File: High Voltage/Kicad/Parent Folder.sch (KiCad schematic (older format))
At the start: 45 parts

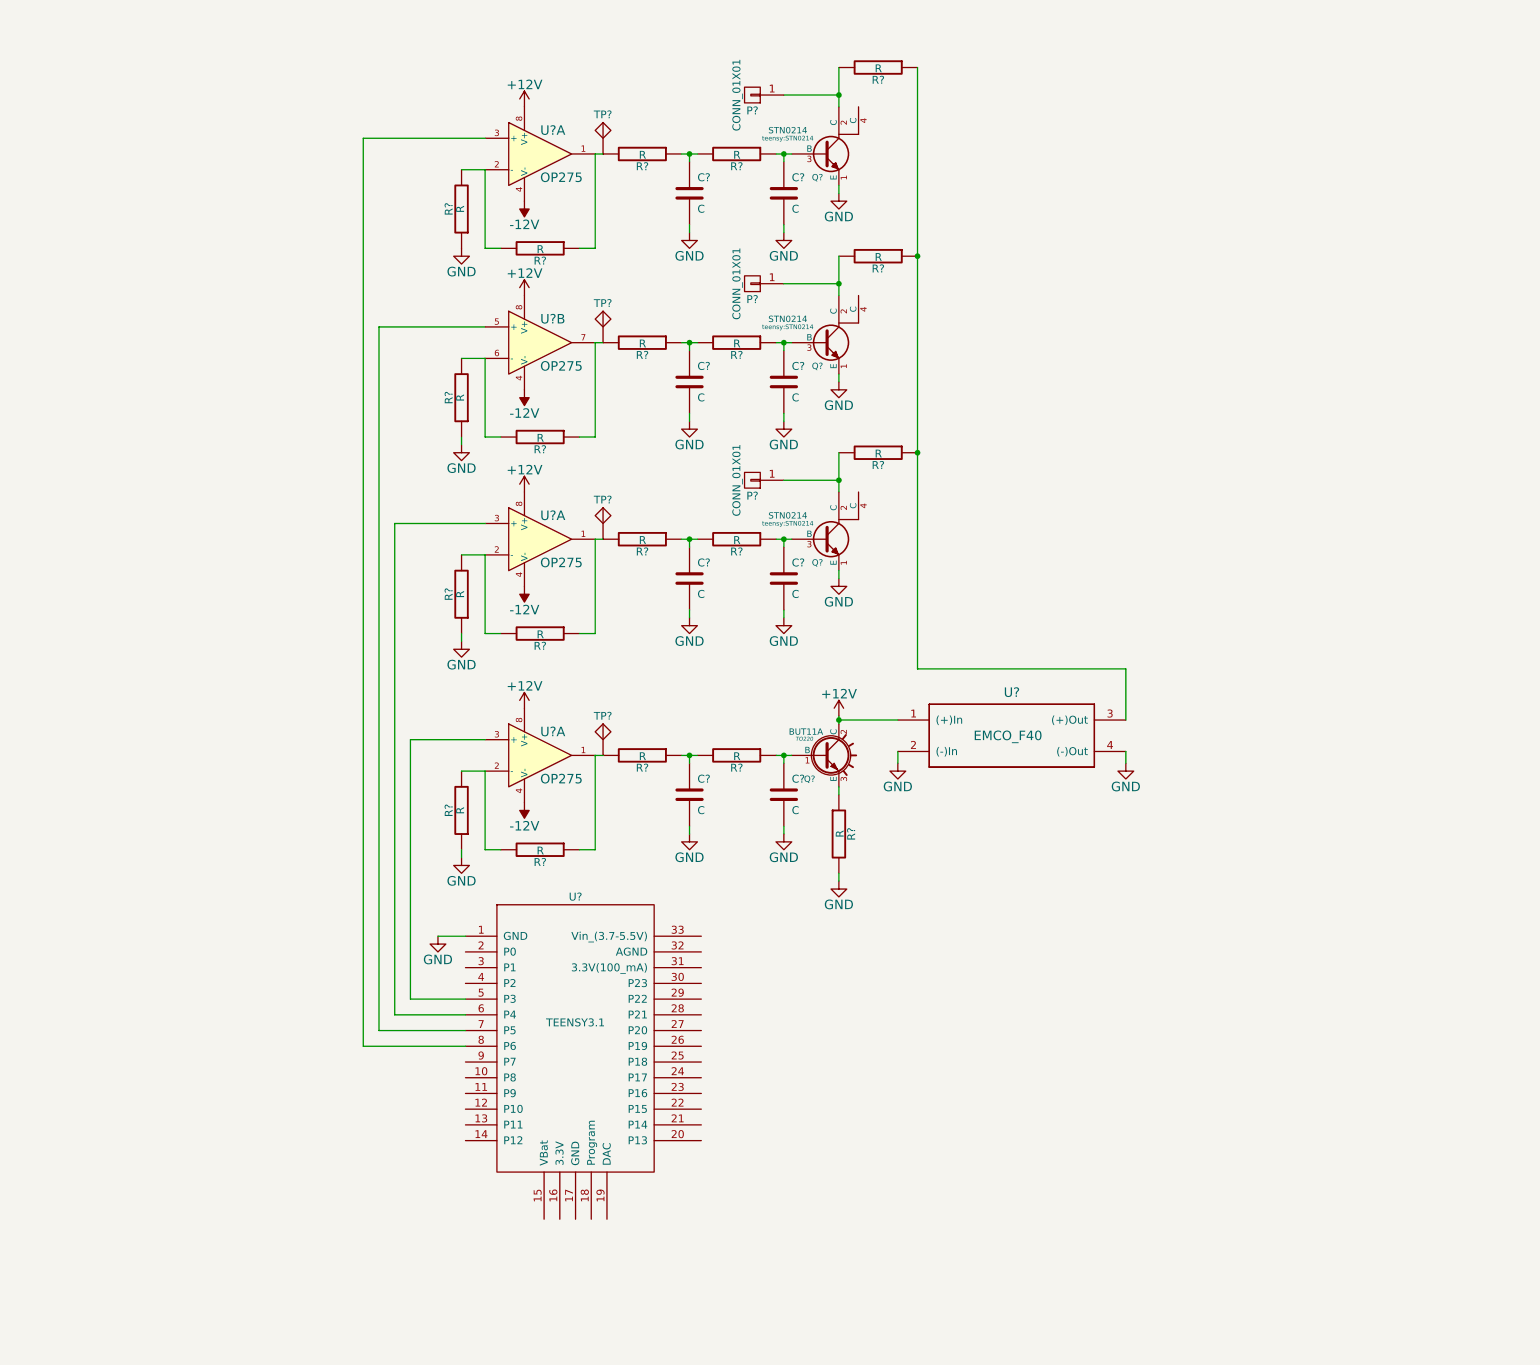
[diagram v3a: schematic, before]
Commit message: HV schematic and layout
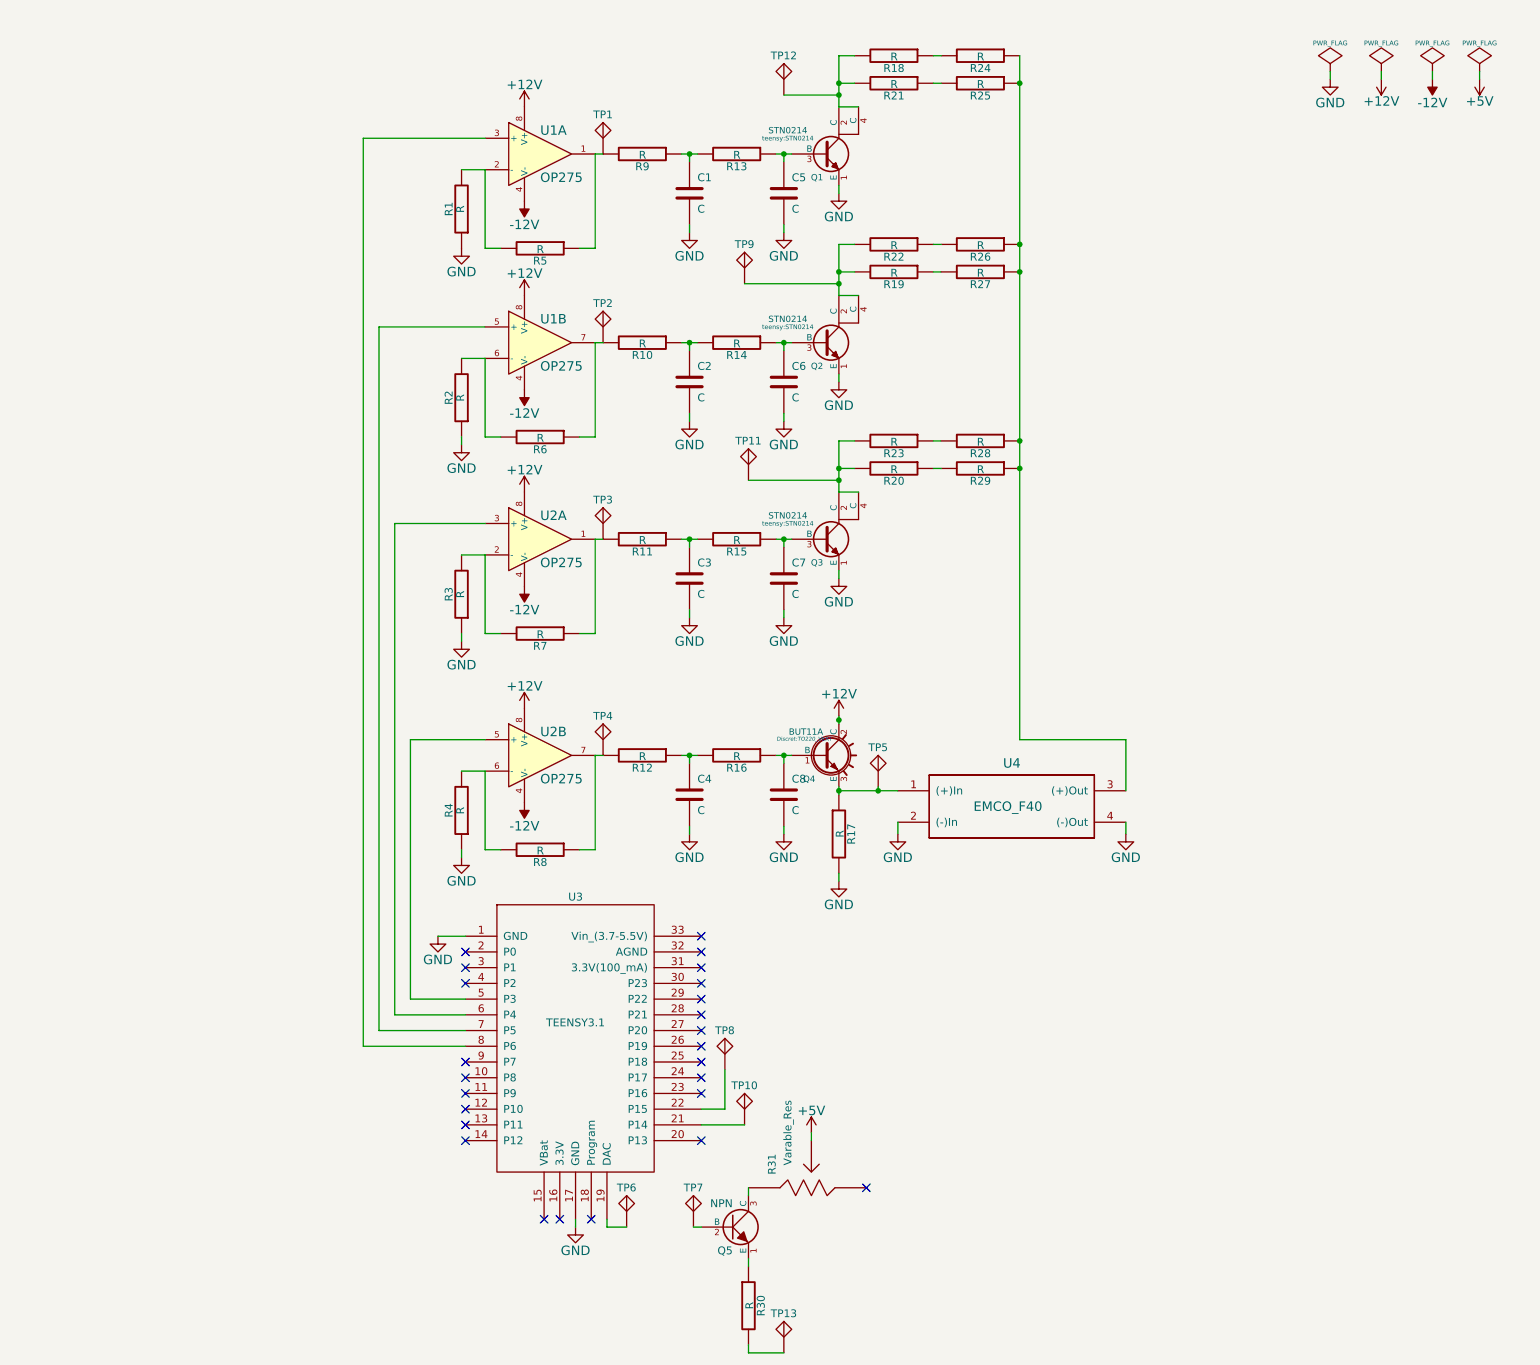
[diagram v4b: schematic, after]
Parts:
- removed P? (x3): CONN_01X01, symbol CONN_01X01
- added Q5: NPN, Discret:TO220_VERT, symbol NPN
- added R21, R22, R23, R24, R25, R26, R27, R28, R29: R, teensy:RES_1W, symbol R
- added R30: R, Resistors_SMD:R_1206_HandSoldering, symbol R
- added R31: Varable_Res, teensy:POT, symbol Varable_Res
- added TP10, TP11, TP12, TP13, TP5, TP6, TP7, TP8, TP9: Test_point, Connect:PINTST, symbol Test_point
- C1, C2, C3, C4, C5, C6, C7, C8: renamed from C?; footprint (none) -> Capacitors_SMD:C_1206_HandSoldering
- Q4: renamed from Q?; footprint TO220 -> Discret:TO220_VERT
- R1, R10, R11, R12, R13, R14, R15, R16, R17, R2, R3, R4, R5, R6, R7, R8, R9: renamed from R?; footprint (none) -> Resistors_SMD:R_1206_HandSoldering
- R18, R19, R20: renamed from R?; footprint (none) -> teensy:RES_1W
- TP1, TP2, TP3, TP4: renamed from TP?; footprint (none) -> Connect:PINTST
- U1, U2: renamed from U?; footprint (none) -> teensy:OpAmp
- U3: renamed from U?; footprint MODULE -> teensy:TEENSY3.1
- U4: renamed from U?; footprint (none) -> teensy:EMCO_F40
- gave numbers to parts that had none: 3
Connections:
- net +12V: no longer U4.1 ((+)In)
- net GND: now also U3.17 (GND)
- net at U3.19 (DAC): now also TP6.1
- net at U3.21 (P14): now also TP10.1
- net at U3.22 (P15): now also TP8.1
- net at U3.5 (P3): now also U2.5 (+); no longer U2.3 (+)
- net at R12.2, R8.1, TP4.1: now also U2.7; no longer U2.1
- net at R4.2, R8.2: now also U2.6 (-); no longer U2.2 (-)
- net at Q1.2 (C), R18.2: now also Q1.4 (C), R21.2, TP12.1
- net at Q2.2 (C), R19.2: now also Q2.4 (C), R22.2, TP9.1
- net at Q3.2 (C), R20.2: now also Q3.4 (C), R23.2, TP11.1
- net at Q4.3 (E), R17.1: now also U4.1 ((+)In), TP5.1
- new net: R19.1, R27.2
- new net: R20.1, R29.2
- new net: R18.1, R24.2
- new net: R24.1, R25.1, R26.1, R27.1, R28.1, R29.1, U4.3 ((+)Out)
- new net: R21.1, R25.2
- new net: R22.1, R26.2
- new net: R23.1, R28.2
- new net: Q5.1 (E), R30.1
- new net: Q5.2 (B), TP7.1
- new net: Q5.3 (C), R31.1
- new net: R30.2, TP13.1
- new net +5V: R31.2
- no-connect marks 0 -> 25
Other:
- moved on the sheet: R18, R19, R20, U4

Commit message: Made a few changes to the board. I think it's ready to be milled
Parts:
- added TP14, TP15, TP16, TP17, TP18, TP19, TP20, TP21, TP22: Test_point, Connect:PINTST, symbol Test_point
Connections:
- net +12V: now also TP16.1, TP17.1, TP18.1
- net +5V: now also TP22.1
- net -12V: now also TP19.1, TP20.1, TP21.1
- net GND: now also TP14.1, TP15.1
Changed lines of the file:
@@
 L GND #PWR025
 U 1 1 550A3571
-P 9750 1025
-F 0 "#PWR025" H 9750 775 60  0001 C CNN
-F 1 "GND" H 9750 875 60  0000 C CNN
-F 2 "" H 9750 1025 60  0000 C CNN
-F 3 "" H 9750 1025 60  0000 C CNN
-	1    9750 1025
+P 8975 1025
+F 0 "#PWR025" H 8975 775 60  0001 C CNN
+F 1 "GND" H 8975 875 60  0000 C CNN
+F 2 "" H 8975 1025 60  0000 C CNN
+F 3 "" H 8975 1025 60  0000 C CNN
+	1    8975 1025
 	1    0    0    -1
 $EndComp
@@
 L PWR_FLAG #FLG026
 U 1 1 550A3585
-P 9750 975
-F 0 "#FLG026" H 9750 1070 30  0001 C CNN
-F 1 "PWR_FLAG" H 9750 1155 30  0000 C CNN
-F 2 "" H 9750 975 60  0000 C CNN
-F 3 "" H 9750 975 60  0000 C CNN
-	1    9750 975
+P 8975 975
+F 0 "#FLG026" H 8975 1070 30  0001 C CNN
+F 1 "PWR_FLAG" H 8975 1155 30  0000 C CNN
+F 2 "" H 8975 975 60  0000 C CNN
+F 3 "" H 8975 975 60  0000 C CNN
+	1    8975 975
 	1    0    0    -1
 $EndComp
@@
 L PWR_FLAG #FLG027
 U 1 1 550A376B
-P 10075 975
-F 0 "#FLG027" H 10075 1070 30  0001 C CNN
-F 1 "PWR_FLAG" H 10075 1155 30  0000 C CNN
-F 2 "" H 10075 975 60  0000 C CNN
-F 3 "" H 10075 975 60  0000 C CNN
-	1    10075 975
+P 9725 975
+F 0 "#FLG027" H 9725 1070 30  0001 C CNN
+F 1 "PWR_FLAG" H 9725 1155 30  0000 C CNN
+F 2 "" H 9725 975 60  0000 C CNN
+F 3 "" H 9725 975 60  0000 C CNN
+	1    9725 975
 	1    0    0    -1
 $EndComp
@@
 L +12V #PWR029
 U 1 1 550A380A
-P 10075 1025
-F 0 "#PWR029" H 10075 875 60  0001 C CNN
-F 1 "+12V" H 10075 1165 60  0000 C CNN
-F 2 "" H 10075 1025 60  0000 C CNN
-F 3 "" H 10075 1025 60  0000 C CNN
-	1    10075 1025
+P 9725 1025
+F 0 "#PWR029" H 9725 875 60  0001 C CNN
+F 1 "+12V" H 9725 1165 60  0000 C CNN
+F 2 "" H 9725 1025 60  0000 C CNN
+F 3 "" H 9725 1025 60  0000 C CNN
+	1    9725 1025
 	-1   0    0    1
 $EndComp
@@
 $EndComp
 Wire Wire Line
-	10075 975  10075 1025
-Wire Wire Line
-	10400 1025 10400 975
+	9725 975  9725 1025
+Wire Wire Line
+	10400 975  10400 1025
 NoConn ~ 4250 7275
 NoConn ~ 4250 7375
@@
 	5150 8275 5150 8325
 Wire Wire Line
-	9750 975  9750 1025
+	8975 975  8975 1025
 $Comp
 L NPN Q5
@@
 Wire Wire Line
 	6050 9125 6275 9125
+$Comp
+L Test_point TP15
+U 1 1 55137624
+P 8750 975
+F 0 "TP15" H 8750 1225 49  0000 C CNN
+F 1 "Test_point" H 8750 1325 49  0001 C CNN
+F 2 "Connect:PINTST" H 8750 975 49  0001 C CNN
+F 3 "" H 8750 975 49  0000 C CNN
+	1    8750 975
+	1    0    0    -1
+$EndComp
+Wire Wire Line
+	8600 975  8975 975
+$Comp
+L Test_point TP14
+U 1 1 5513C29A
+P 8600 975
+F 0 "TP14" H 8600 1225 49  0000 C CNN
+F 1 "Test_point" H 8600 1325 49  0001 C CNN
+F 2 "Connect:PINTST" H 8600 975 49  0001 C CNN
+F 3 "" H 8600 975 49  0000 C CNN
+	1    8600 975
+	1    0    0    -1
+$EndComp
+Connection ~ 8750 975
+$Comp
+L Test_point TP16
+U 1 1 5513C3C8
+P 9225 975
+F 0 "TP16" H 9225 1225 49  0000 C CNN
+F 1 "Test_point" H 9225 1325 49  0001 C CNN
+F 2 "Connect:PINTST" H 9225 975 49  0001 C CNN
+F 3 "" H 9225 975 49  0000 C CNN
+	1    9225 975
+	1    0    0    -1
+$EndComp
+$Comp
+L Test_point TP17
+U 1 1 5513C43E
+P 9375 975
+F 0 "TP17" H 9375 1225 49  0000 C CNN
+F 1 "Test_point" H 9375 1325 49  0001 C CNN
+F 2 "Connect:PINTST" H 9375 975 49  0001 C CNN
+F 3 "" H 9375 975 49  0000 C CNN
+	1    9375 975
+	1    0    0    -1
+$EndComp
+$Comp
+L Test_point TP18
+U 1 1 5513C49D
+P 9525 975
+F 0 "TP18" H 9525 1225 49  0000 C CNN
+F 1 "Test_point" H 9525 1325 49  0001 C CNN
+F 2 "Connect:PINTST" H 9525 975 49  0001 C CNN
+F 3 "" H 9525 975 49  0000 C CNN
+	1    9525 975
+	1    0    0    -1
+$EndComp
+Wire Wire Line
+	9225 975  9725 975
+Connection ~ 9375 975
+Connection ~ 9525 975
+$Comp
+L Test_point TP19
+U 1 1 5513C992
+P 9925 975
+F 0 "TP19" H 9925 1225 49  0000 C CNN
+F 1 "Test_point" H 9925 1325 49  0001 C CNN
+F 2 "Connect:PINTST" H 9925 975 49  0001 C CNN
+F 3 "" H 9925 975 49  0000 C CNN
+	1    9925 975
+	1    0    0    -1
+$EndComp
+$Comp
+L Test_point TP20
+U 1 1 5513CA0F
+P 10075 975
+F 0 "TP20" H 10075 1225 49  0000 C CNN
+F 1 "Test_point" H 10075 1325 49  0001 C CNN
+F 2 "Connect:PINTST" H 10075 975 49  0001 C CNN
+F 3 "" H 10075 975 49  0000 C CNN
+	1    10075 975
+	1    0    0    -1
+$EndComp
+$Comp
+L Test_point TP21
+U 1 1 5513CA71
+P 10225 975
+F 0 "TP21" H 10225 1225 49  0000 C CNN
+F 1 "Test_point" H 10225 1325 49  0001 C CNN
+F 2 "Connect:PINTST" H 10225 975 49  0001 C CNN
+F 3 "" H 10225 975 49  0000 C CNN
+	1    10225 975
+	1    0    0    -1
+$EndComp
+Wire Wire Line
+	9925 975  10400 975
+Connection ~ 10225 975
+Connection ~ 10075 975
+$Comp
+L Test_point TP22
+U 1 1 5513CD5B
+P 10900 975
+F 0 "TP22" H 10900 1225 49  0000 C CNN
+F 1 "Test_point" H 10900 1325 49  0001 C CNN
+F 2 "Connect:PINTST" H 10900 975 49  0001 C CNN
+F 3 "" H 10900 975 49  0000 C CNN
+	1    10900 975
+	1    0    0    -1
+$EndComp
+Wire Wire Line
+	10900 975  10700 975
+$Comp
+L PWR_FLAG #FLG034
+U 1 1 55143CAB
+P 6450 1100
+F 0 "#FLG034" H 6450 1195 30  0001 C CNN
+F 1 "PWR_FLAG" H 6450 1280 30  0000 C CNN
+F 2 "" H 6450 1100 60  0000 C CNN
+F 3 "" H 6450 1100 60  0000 C CNN
+	1    6450 1100
+	1    0    0    -1
+$EndComp
+$Comp
+L PWR_FLAG #FLG035
+U 1 1 55143CFE
+P 6500 2300
+F 0 "#FLG035" H 6500 2395 30  0001 C CNN
+F 1 "PWR_FLAG" H 6500 2480 30  0000 C CNN
+F 2 "" H 6500 2300 60  0000 C CNN
+F 3 "" H 6500 2300 60  0000 C CNN
+	1    6500 2300
+	1    0    0    -1
+$EndComp
+$Comp
+L PWR_FLAG #FLG036
+U 1 1 55143E71
+P 6500 3550
+F 0 "#FLG036" H 6500 3645 30  0001 C CNN
+F 1 "PWR_FLAG" H 6500 3730 30  0000 C CNN
+F 2 "" H 6500 3550 60  0000 C CNN
+F 3 "" H 6500 3550 60  0000 C CNN
+	1    6500 3550
+	1    0    0    -1
+$EndComp
+Wire Wire Line
+	6450 1100 6450 1125
+Connection ~ 6450 1125
+Wire Wire Line
+	6500 2300 6500 2325
+Connection ~ 6500 2325
+Wire Wire Line
+	6500 3550 6500 3575
+Connection ~ 6500 3575
 $EndSCHEMATC
